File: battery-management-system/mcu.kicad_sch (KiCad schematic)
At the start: 2 parts, among them U4 STM32L071CZTx, U5 ARM-JTAG-SWD

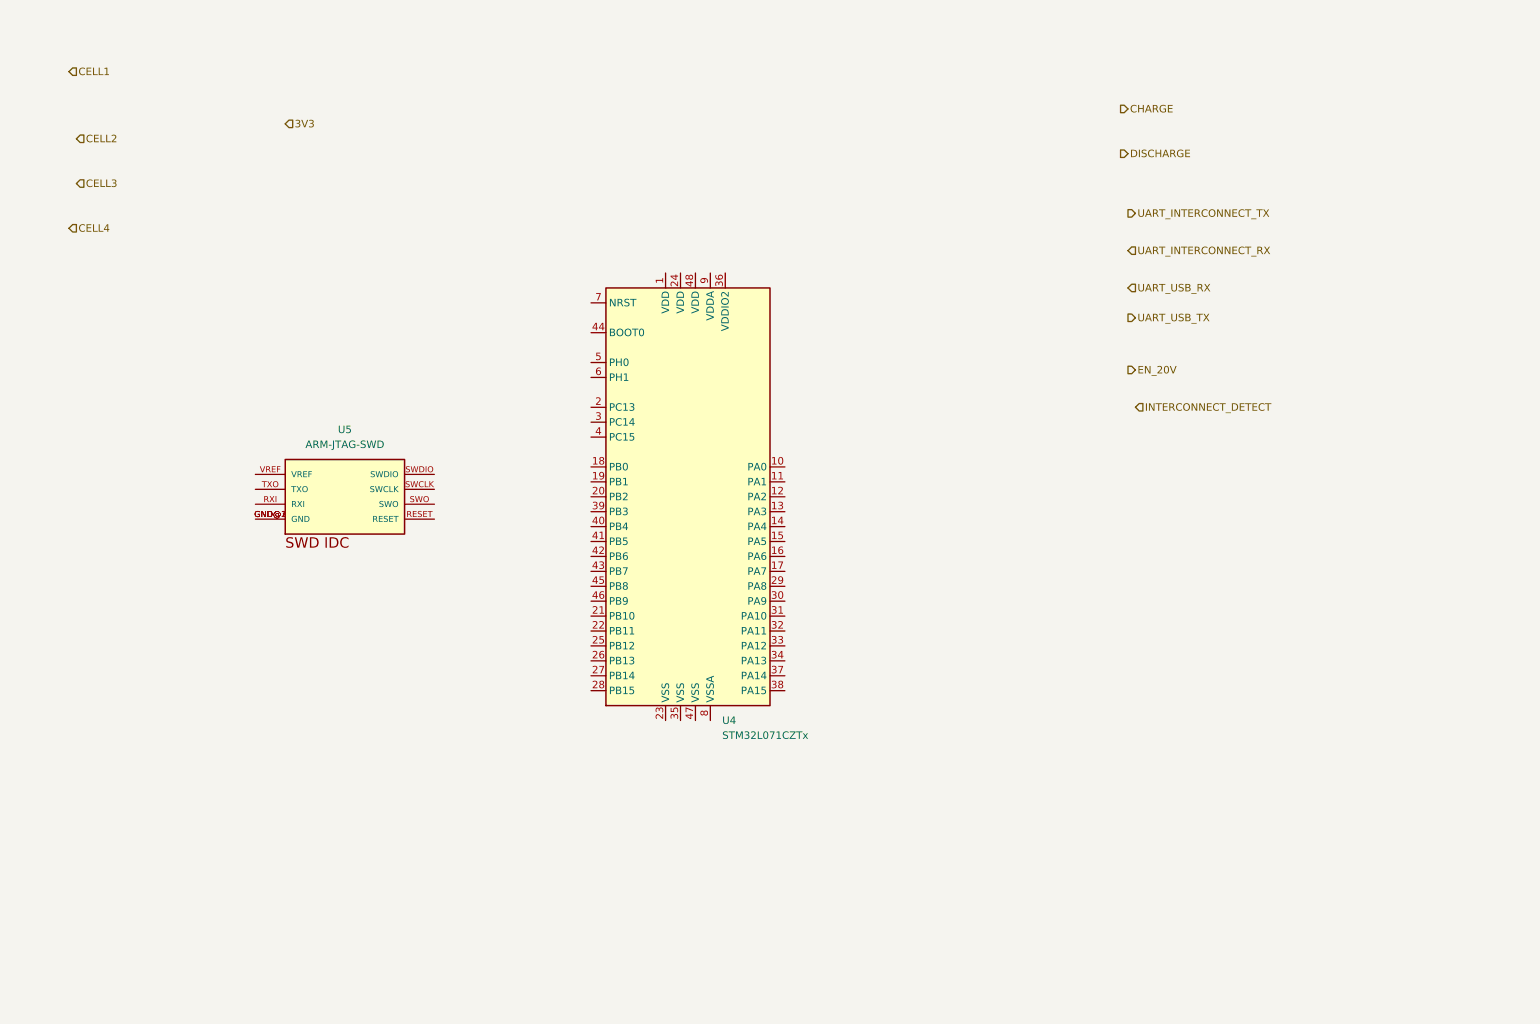
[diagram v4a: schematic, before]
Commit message: route UART and ADC channels on MCU
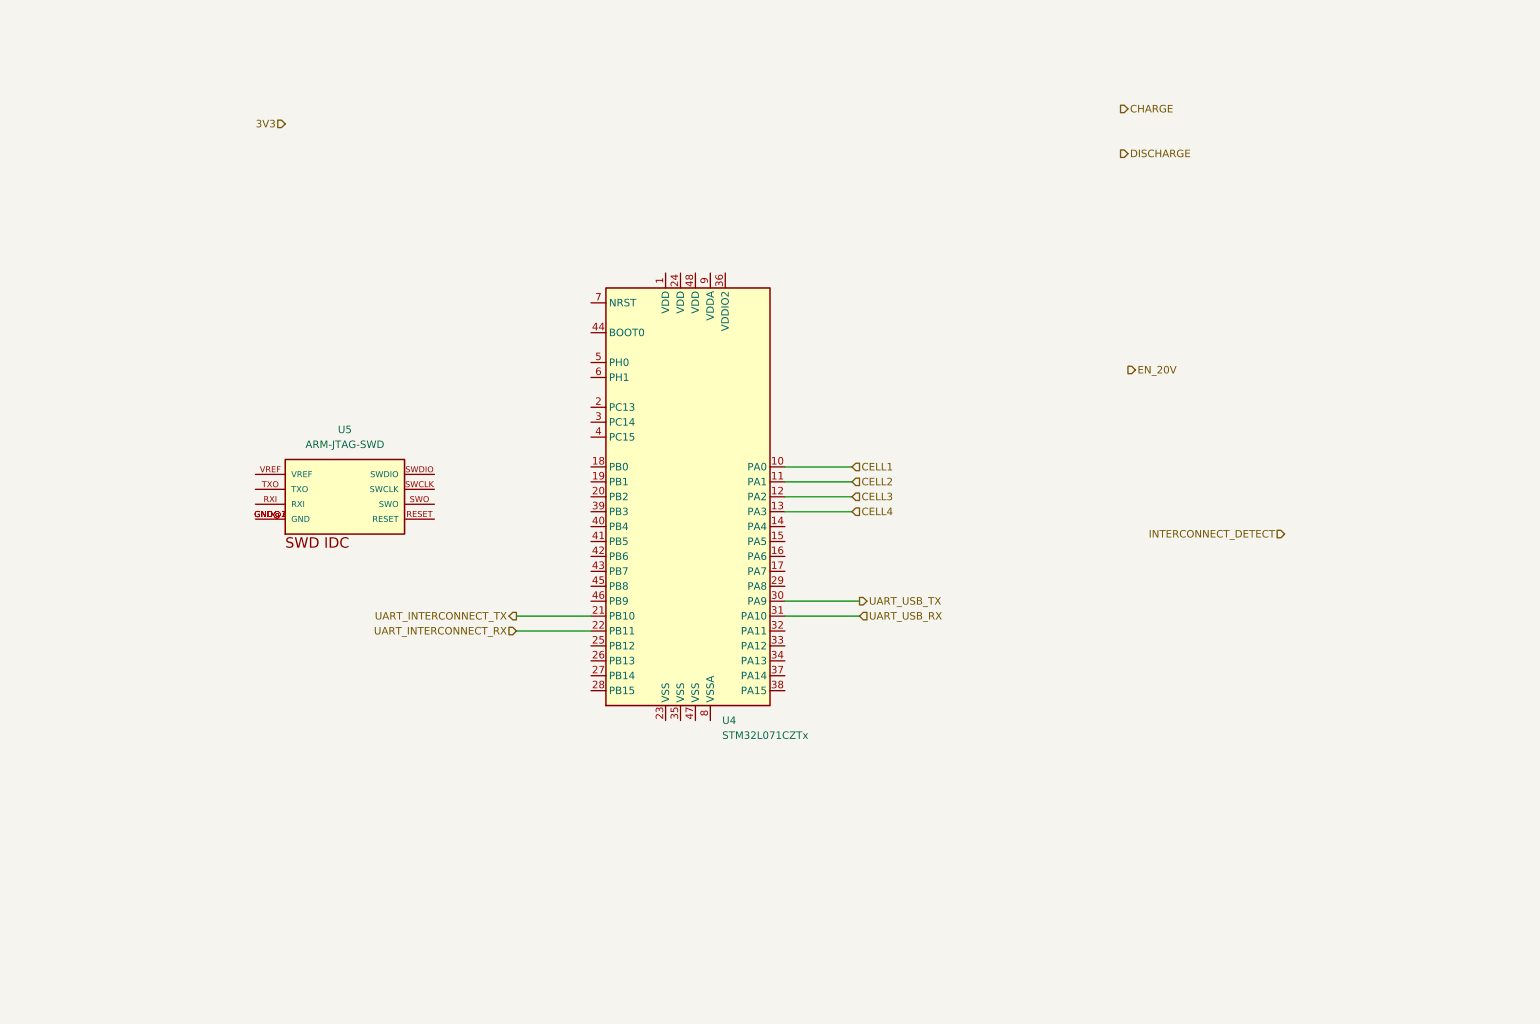
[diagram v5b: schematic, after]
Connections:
- net CELL1: now also U4.10 (PA0)
- net CELL2: now also U4.11 (PA1)
- net CELL3: now also U4.12 (PA2)
- net CELL4: now also U4.13 (PA3)
- net UART_INTERCONNECT_RX: now also U4.22 (PB11)
- net UART_INTERCONNECT_TX: now also U4.21 (PB10)
- net UART_USB_RX: now also U4.31 (PA10)
- net UART_USB_TX: now also U4.30 (PA9)
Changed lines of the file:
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@@
 (kicad_sch (version 20211123) (generator eeschema)
   (paper "A4")
-  (hierarchical_label "INTERCONNECT_DETECT" (shape input) (at 209.55 88.9 0)
-    (effects (font (size 1.27 1.27)) (justify left))
+  (wire (pts (xy 104.14 127) (xy 116.84 127))
+    (stroke (width 0) (type default) (color 0 0 0 0))
   )
-  (hierarchical_label "UART_USB_TX" (shape output) (at 208.28 73.66 0)
+  (wire (pts (xy 149.86 106.68) (xy 161.29 106.68))
+    (stroke (width 0) (type default) (color 0 0 0 0))
+  )
+  (wire (pts (xy 149.86 104.14) (xy 161.29 104.14))
+    (stroke (width 0) (type default) (color 0 0 0 0))
+  )
+  (wire (pts (xy 149.86 121.92) (xy 162.56 121.92))
+    (stroke (width 0) (type default) (color 0 0 0 0))
+  )
+  (wire (pts (xy 104.14 124.46) (xy 116.84 124.46))
+    (stroke (width 0) (type default) (color 0 0 0 0))
+  )
+  (wire (pts (xy 149.86 124.46) (xy 162.56 124.46))
+    (stroke (width 0) (type default) (color 0 0 0 0))
+  )
+  (wire (pts (xy 149.86 99.06) (xy 161.29 99.06))
+    (stroke (width 0) (type default) (color 0 0 0 0))
+  )
+  (wire (pts (xy 149.86 101.6) (xy 161.29 101.6))
+    (stroke (width 0) (type default) (color 0 0 0 0))
+  )
+  (hierarchical_label "INTERCONNECT_DETECT" (shape input) (at 234.95 110.49 180)
+    (effects (font (size 1.27 1.27)) (justify right))
+  )
+  (hierarchical_label "UART_USB_TX" (shape output) (at 162.56 121.92 0)
     (effects (font (size 1.27 1.27)) (justify left))
   )
@@
     (effects (font (size 1.27 1.27)) (justify left))
   )
-  (hierarchical_label "3V3" (shape input) (at 64.77 40.64 0)
+  (hierarchical_label "3V3" (shape input) (at 64.77 40.64 180)
+    (effects (font (size 1.27 1.27)) (justify right))
+  )
+  (hierarchical_label "UART_USB_RX" (shape input) (at 162.56 124.46 0)
     (effects (font (size 1.27 1.27)) (justify left))
   )
-  (hierarchical_label "UART_USB_RX" (shape input) (at 208.28 68.58 0)
+  (hierarchical_label "CELL1" (shape input) (at 161.29 99.06 0)
     (effects (font (size 1.27 1.27)) (justify left))
   )
-  (hierarchical_label "CELL1" (shape input) (at 27.94 31.75 0)
-    (effects (font (size 1.27 1.27)) (justify left))
+  (hierarchical_label "UART_INTERCONNECT_RX" (shape input) (at 104.14 127 180)
+    (effects (font (size 1.27 1.27)) (justify right))
   )
-  (hierarchical_label "UART_INTERCONNECT_RX" (shape input) (at 208.28 62.23 0)
-    (effects (font (size 1.27 1.27)) (justify left))
-  )
-  (hierarchical_label "CELL4" (shape input) (at 27.94 58.42 0)
+  (hierarchical_label "CELL4" (shape input) (at 161.29 106.68 0)
     (effects (font (size 1.27 1.27)) (justify left))
   )
@@
     (effects (font (size 1.27 1.27)) (justify left))
   )
-  (hierarchical_label "UART_INTERCONNECT_TX" (shape output) (at 208.28 55.88 0)
-    (effects (font (size 1.27 1.27)) (justify left))
+  (hierarchical_label "UART_INTERCONNECT_TX" (shape output) (at 104.14 124.46 180)
+    (effects (font (size 1.27 1.27)) (justify right))
   )
-  (hierarchical_label "CELL3" (shape input) (at 29.21 50.8 0)
+  (hierarchical_label "CELL3" (shape input) (at 161.29 104.14 0)
     (effects (font (size 1.27 1.27)) (justify left))
   )
@@
     (effects (font (size 1.27 1.27)) (justify left))
   )
-  (hierarchical_label "CELL2" (shape input) (at 29.21 43.18 0)
+  (hierarchical_label "CELL2" (shape input) (at 161.29 101.6 0)
     (effects (font (size 1.27 1.27)) (justify left))
   )

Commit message: add power supply for MCU
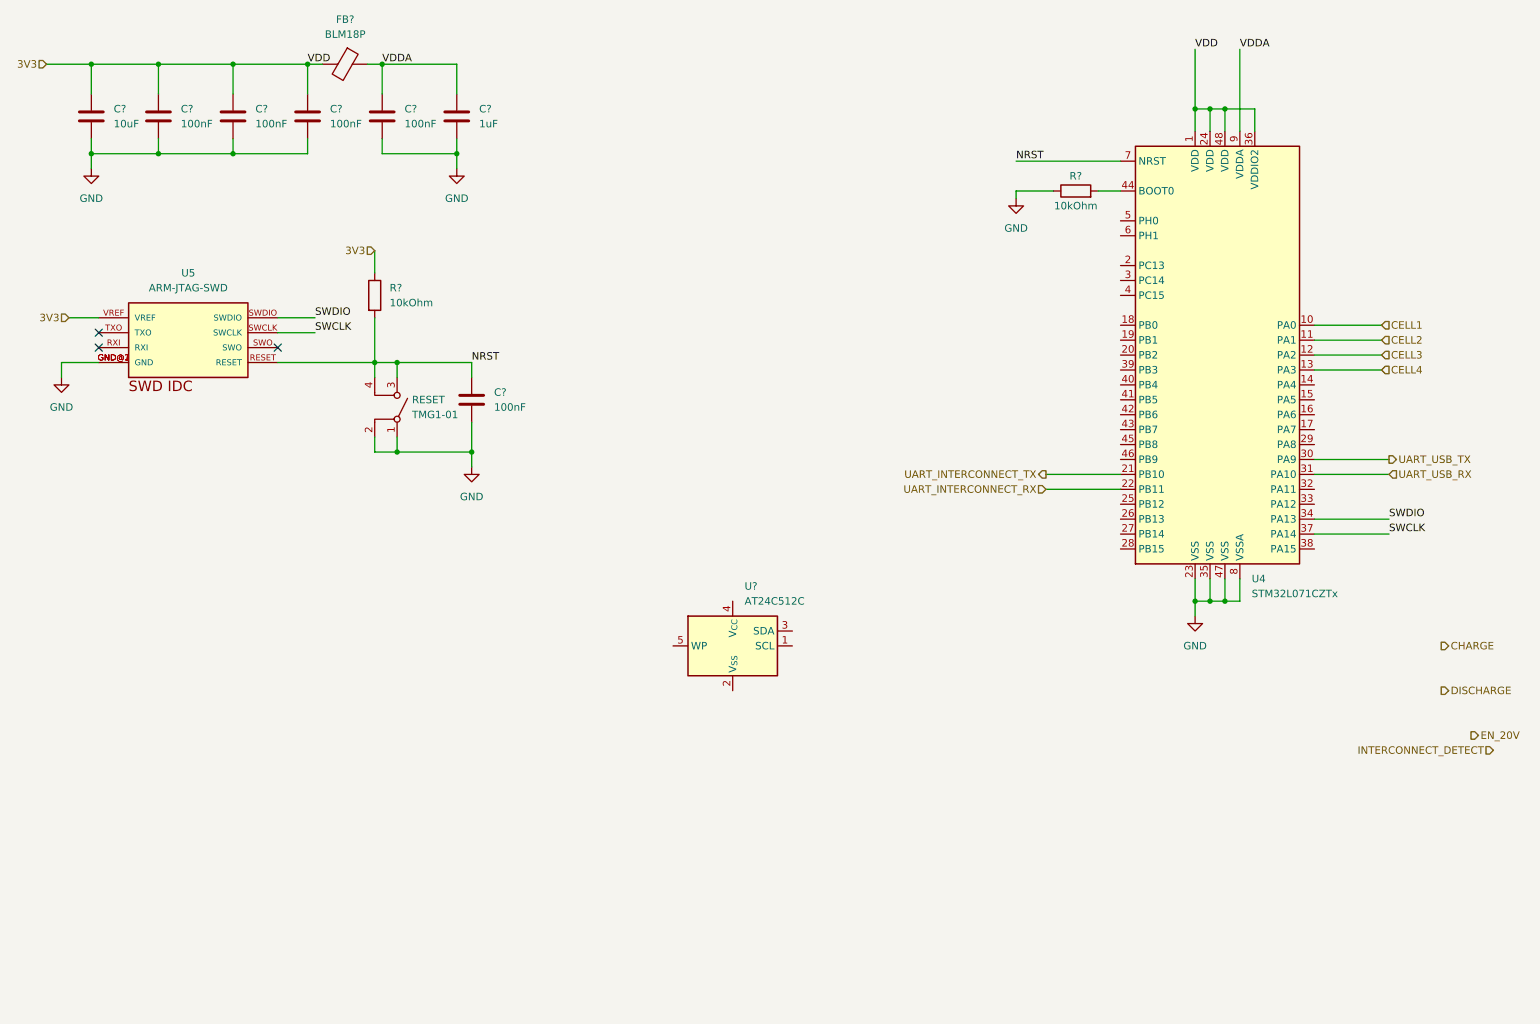
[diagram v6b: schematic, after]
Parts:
- added C?: 1uF, benediktibk:C_0603_1608Metric_Pad1.08x0.95mm_HandSolder, symbol benediktibk:C_1uF_SMD_0603_50V_10%
- added C? (x5): 100nF, benediktibk:C_0603_1608Metric_Pad1.08x0.95mm_HandSolder, symbol benediktibk:C_100nF_SMD_0603_50V
- added C?: 10uF, benediktibk:C_1210_3225Metric_Pad1.33x2.70mm_HandSolder, symbol benediktibk:C_10uF_SMD_1210_50V_20%
- added FB?: BLM18P, benediktibk:R_0603_1608Metric_Pad0.98x0.95mm_HandSolder, symbol benediktibk:BLM18P
- added R? (x2): 10kOhm, benediktibk:R_0603_1608Metric_Pad0.98x0.95mm_HandSolder, symbol benediktibk:R_10kOhm_SMD_0603_100mW_1%
- added RESET: TMG1-01, benediktibk:TMG1-01, symbol benediktibk:TMG1-01
- added U?: AT24C512C, benediktibk:SOIC-8_3.9x4.9mm_P1.27mm, symbol benediktibk:AT24C512C
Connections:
- net 3V3: now also U4.1 (VDD), U4.24 (VDD), U4.36 (VDDIO2), U4.48 (VDD), U5.VREF, C?.1, C?.1, C?.1, C?.1, FB?.2, R?.1
- net GND: now reaches U4.23 (VSS)
- net GND: now also U4.35 (VSS), U4.47 (VSS), U4.8 (VSSA), U5.GND@1 (GND), U5.GND@2 (GND), U5.GND@3 (GND), C?.2, C?.2, C?.2, C?.2, C?.2, C?.2, C?.2, R?.1, RESET.1 (A), RESET.2 (A)
- net SWDIO: now reaches U4.34 (PA13)
- net SWDIO: now also U5.SWDIO
- net SWCLK: now reaches U4.37 (PA14)
- net SWCLK: now also U5.SWCLK
- net at U4.44 (BOOT0): now also R?.2
- net NRST: now reaches U4.7 (NRST)
- net NRST: now also U5.RESET, C?.1, R?.2, RESET.3 (B), RESET.4 (B)
- net VDDA: now reaches U4.9 (VDDA)
- net VDDA: now also C?.1, C?.1, FB?.1
- no-connect marks 0 -> 3
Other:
- moved on the sheet: U4, U5

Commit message: add temperature sensor and LEDs
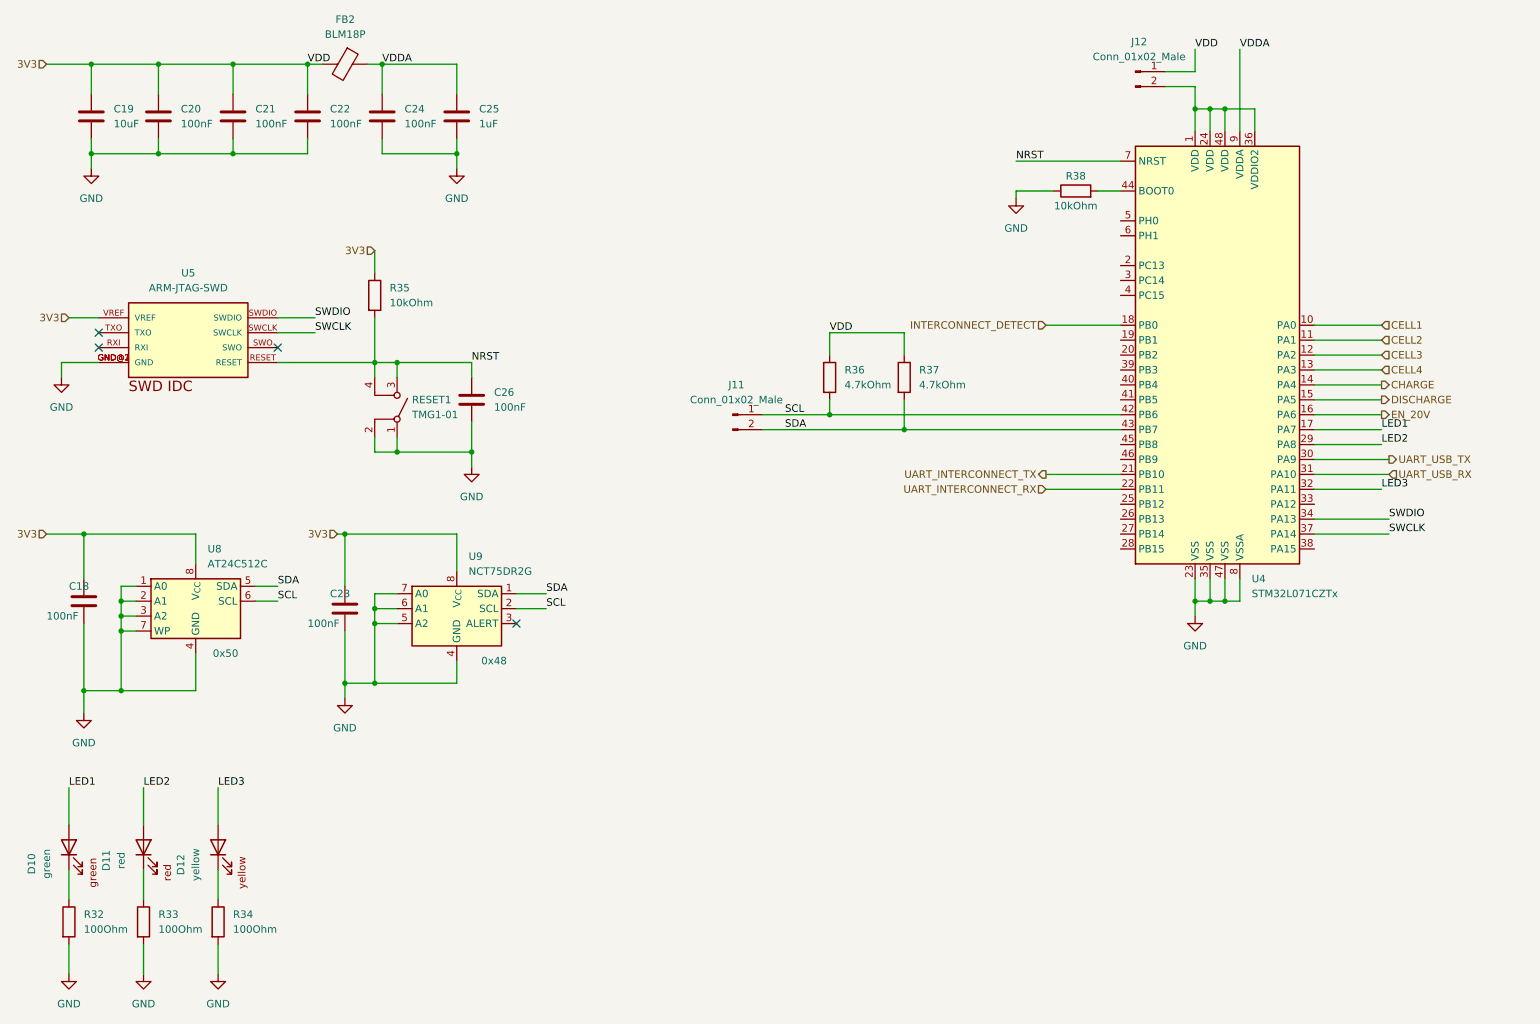
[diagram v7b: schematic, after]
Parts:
- added C18, C23: 100nF, benediktibk:C_0603_1608Metric_Pad1.08x0.95mm_HandSolder, symbol benediktibk:C_100nF_SMD_0603_50V
- added D10: green, benediktibk:D_0603_1608Metric_Pad1.05x0.95mm_HandSolder, symbol benediktibk:LED_green_0603
- added D11: red, benediktibk:D_0603_1608Metric_Pad1.05x0.95mm_HandSolder, symbol benediktibk:LED_red_0603
- added D12: yellow, benediktibk:D_0603_1608Metric_Pad1.05x0.95mm_HandSolder, symbol benediktibk:LED_yellow_0603
- added J11, J12: Conn_01x02_Male, benediktibk:PinHeader_1x02_P2.54mm_Vertical, symbol benediktibk:Conn_01x02_Male
- added R32, R33, R34: 100Ohm, benediktibk:R_0603_1608Metric_Pad0.98x0.95mm_HandSolder, symbol benediktibk:R_100Ohm_SMD_0603_100mW_1%
- added R36, R37: 4.7kOhm, benediktibk:R_0603_1608Metric_Pad0.98x0.95mm_HandSolder, symbol benediktibk:R_4_7kOhm_SMD_0603_100mW_1%
- added U9: NCT75DR2G, benediktibk:SOIC-8_3.9x4.9mm_P1.27mm, symbol benediktibk:NCT75DR2G
- U8: renamed from U?; I2C Address (none) -> 0x50; RS order number 236-8814 -> 197-5331
- gave numbers to parts that had none: 10
- renumbered RESET to RESET1
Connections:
- net 3V3: now also U8.8 (V_{CC}), C18.1, C23.1, J12.1 (Pin_1), R36.1, R37.1, U9.8 (V_{CC}); no longer U4.1 (VDD), U4.24 (VDD), U4.36 (VDDIO2), U4.48 (VDD)
- net CHARGE: now also U4.14 (PA4)
- net DISCHARGE: now also U4.15 (PA5)
- net EN_20V: now also U4.16 (PA6)
- net GND: now also U8.1 (A0), U8.2 (A1), U8.3 (A2), U8.4 (GND), U8.7 (WP), C18.2, C23.2, R32.2, R33.2, R34.2, U9.4 (GND), U9.5 (A2), U9.6 (A1), U9.7 (A0)
- net INTERCONNECT_DETECT: now also U4.18 (PB0)
- net LED1: now reaches U4.17 (PA7)
- net LED1: now also D10.2 (A)
- net LED2: now reaches U4.29 (PA8)
- net LED2: now also D11.2 (A)
- net LED3: now reaches U4.32 (PA11)
- net LED3: now also D12.2 (A)
- net SCL: now reaches U4.42 (PB6)
- net SCL: now also U8.6 (SCL), J11.1 (Pin_1), R36.2, U9.2 (SCL)
- net SDA: now reaches U4.43 (PB7)
- net SDA: now also U8.5 (SDA), J11.2 (Pin_2), R37.2, U9.1 (SDA)
- new net: D10.1 (K), R32.1
- new net: D12.1 (K), R34.1
- new net: J12.2 (Pin_2), U4.1 (VDD), U4.24 (VDD), U4.36 (VDDIO2), U4.48 (VDD)
- new net: D11.1 (K), R33.1
- no-connect marks 3 -> 4

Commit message: add components
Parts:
- added J13: LEDS, benediktibk:PinHeader_1x04_P2.54mm_Vertical, symbol benediktibk:Conn_01x04
- J11: value Conn_01x02_Male -> I2C; footprint benediktibk:PinHeader_1x02_P2.54mm_Vertical -> benediktibk:PinHeader_1x03_P2.54mm_Vertical; symbol benediktibk:Conn_01x02_Male -> benediktibk:Conn_01x03; RS order number 251-8086 -> 251-8092
- J12: value Conn_01x02_Male -> MCU_SUPPLY; footprint benediktibk:PinHeader_1x02_P2.54mm_Vertical -> benediktibk:PinHeader_1x03_P2.54mm_Vertical; symbol benediktibk:Conn_01x02_Male -> benediktibk:Conn_01x03; RS order number 251-8086 -> 251-8092
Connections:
- net CHARGE: now also U4.27 (PB14); no longer U4.14 (PA4)
- net DISCHARGE: now also U4.28 (PB15); no longer U4.15 (PA5)
- net GND: now also J11.3 (Pin_3), J12.3 (Pin_3), J13.4 (Pin_4)
- net LED1: now also J13.1 (Pin_1)
- net LED2: now also J13.2 (Pin_2)
- net LED3: now also J13.3 (Pin_3)
- net INTERCONNECT_DETECT: no longer names the net of U4.18 (PB0)
- new net BALANCE_CAP: U4.14 (PA4)
